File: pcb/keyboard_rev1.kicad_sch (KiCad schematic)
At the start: 9 parts

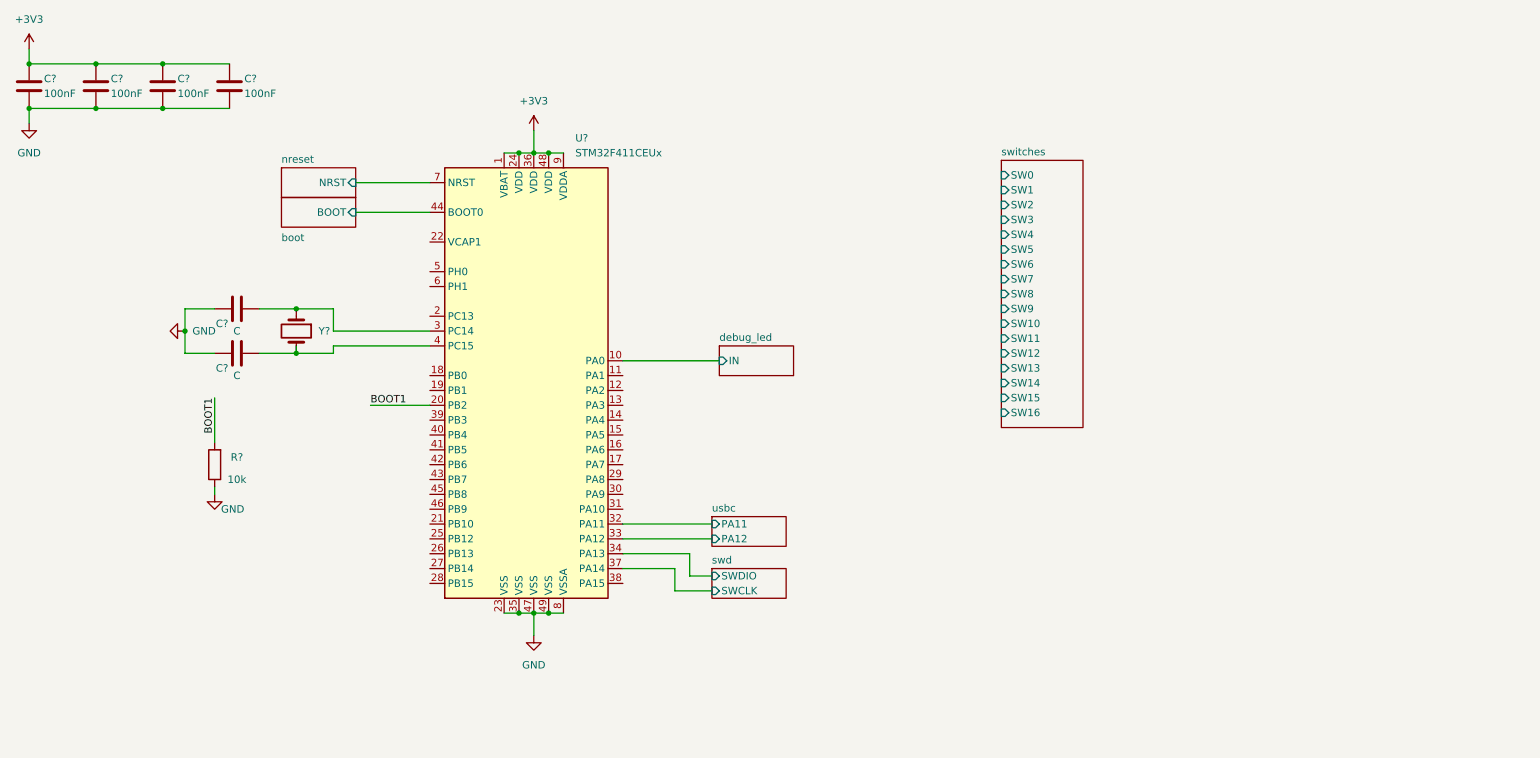
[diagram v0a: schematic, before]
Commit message: Add power (batt, buck+boost) and esp32 BT module (C6).
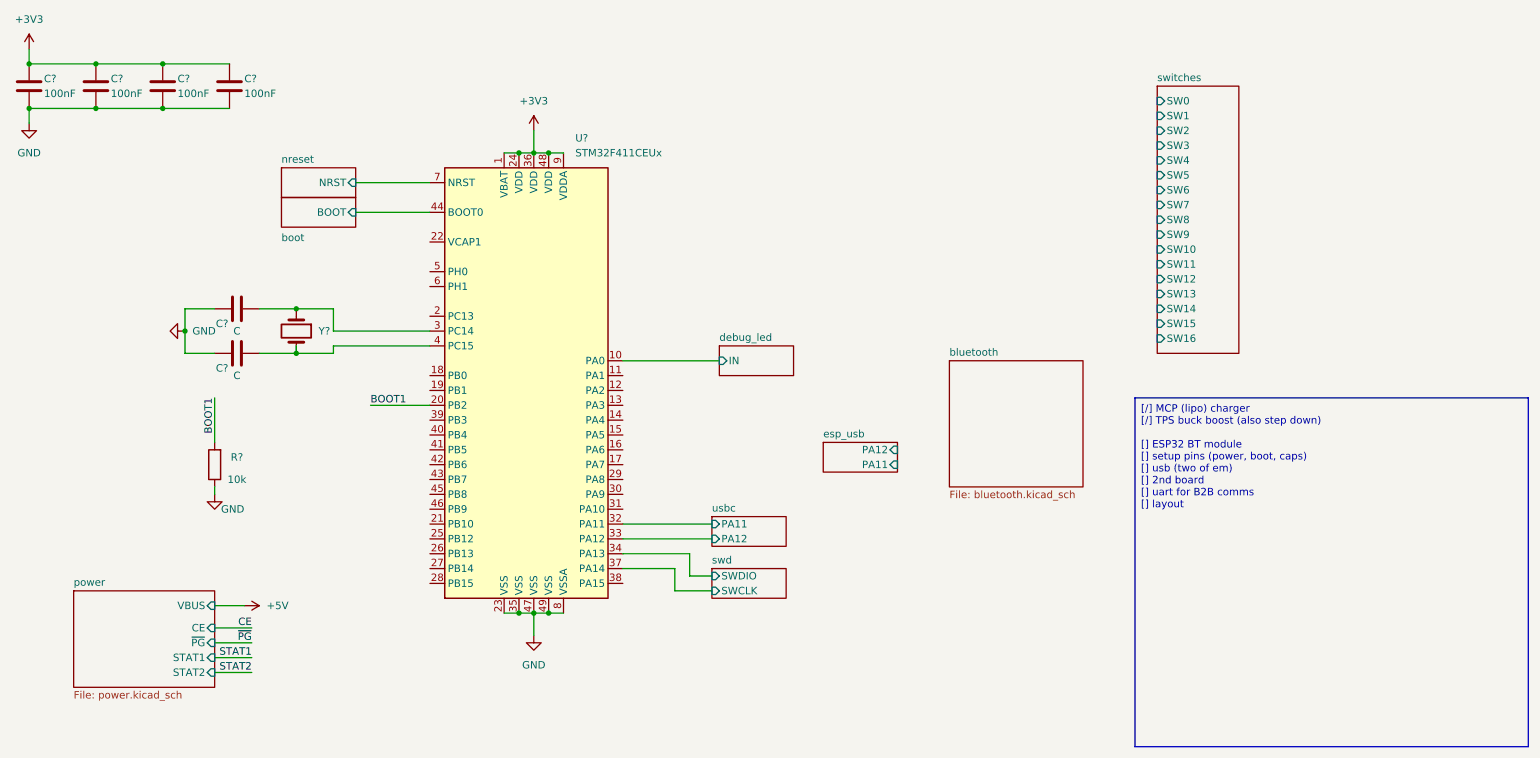
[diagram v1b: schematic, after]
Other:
- added sheet bluetooth (bluetooth.kicad_sch)
- added sheet esp_usb (usbc.kicad_sch)
- added sheet power (power.kicad_sch)
